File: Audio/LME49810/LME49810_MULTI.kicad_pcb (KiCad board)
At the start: 2 copper layers, 165.1 x 190.5 mm, 124 parts, among them Q1 NPN(TO-3P-BCE), Q2 PNP(TO-3P-BCE), Q3 NPN(TO-220-BCE), U1 LME49810

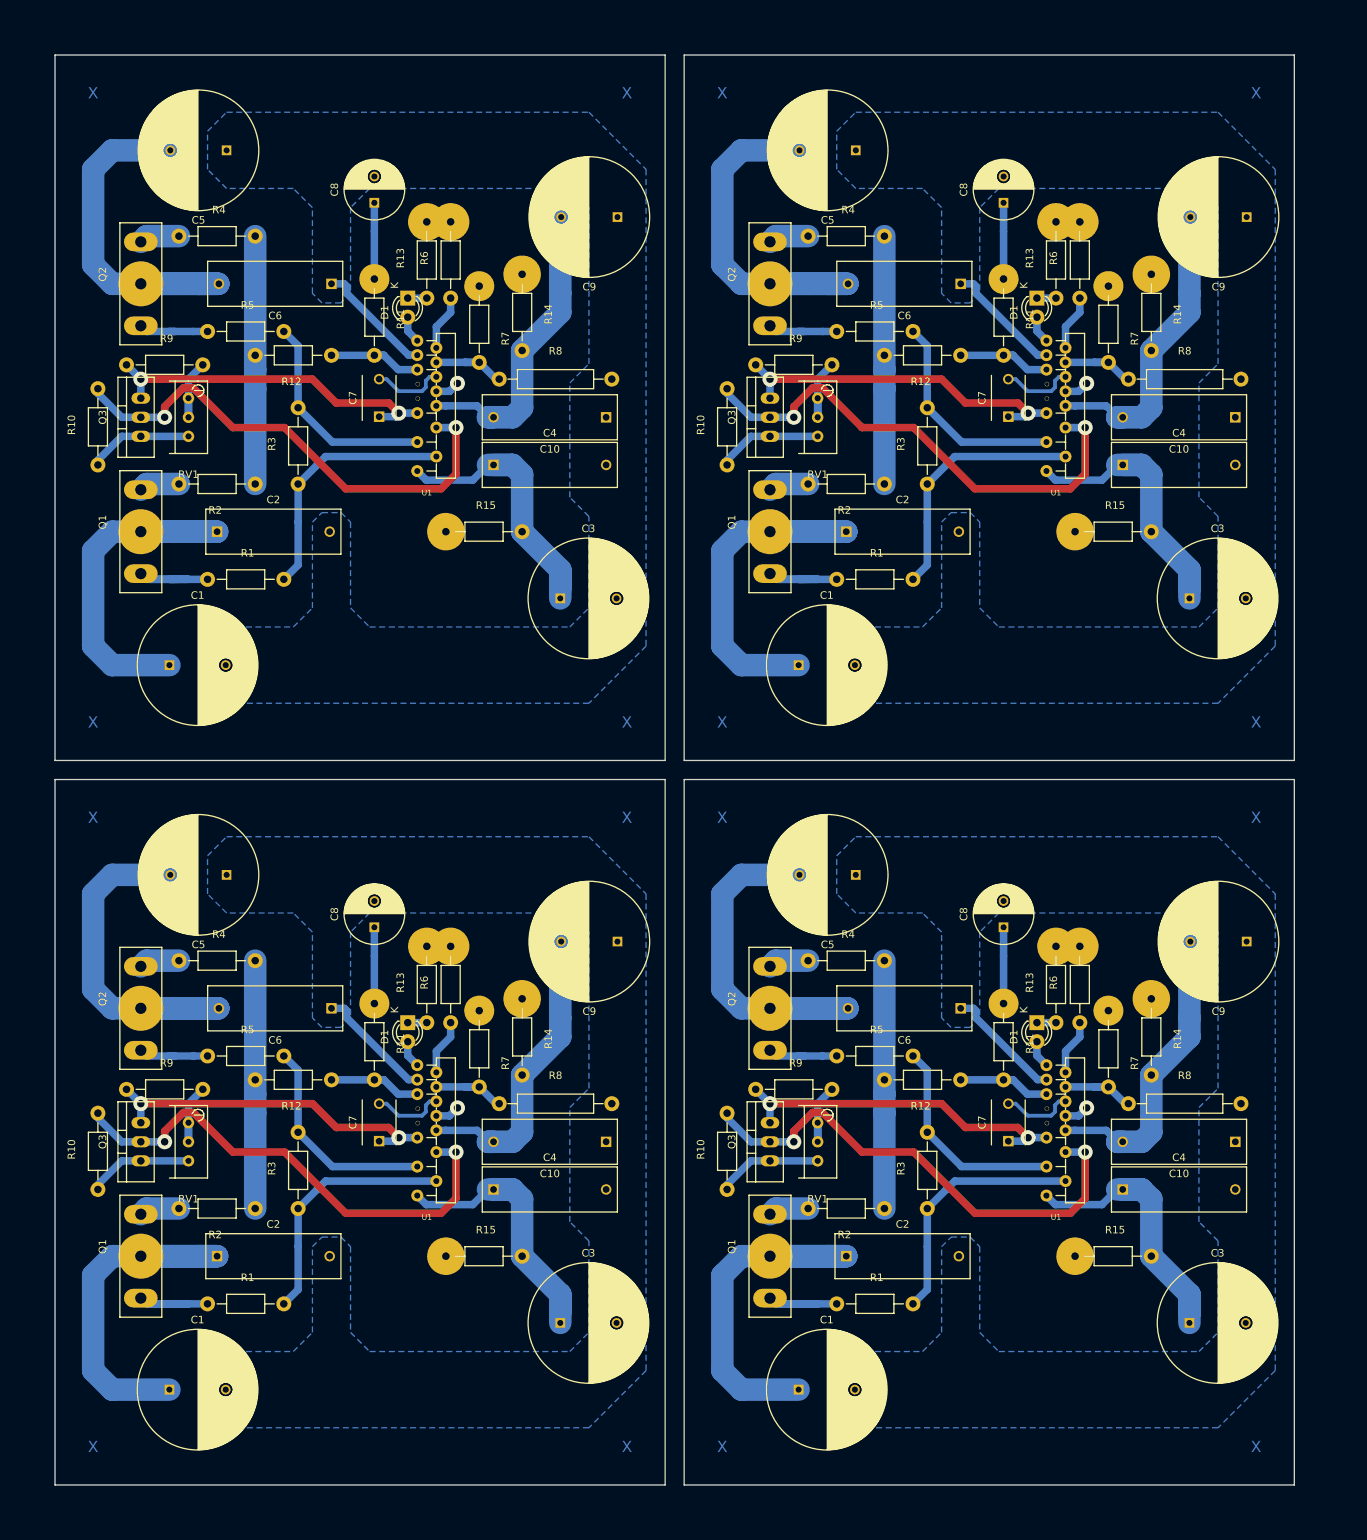
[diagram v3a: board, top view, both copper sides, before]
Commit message: Fixes on component conflict
LME49810 PCB revised
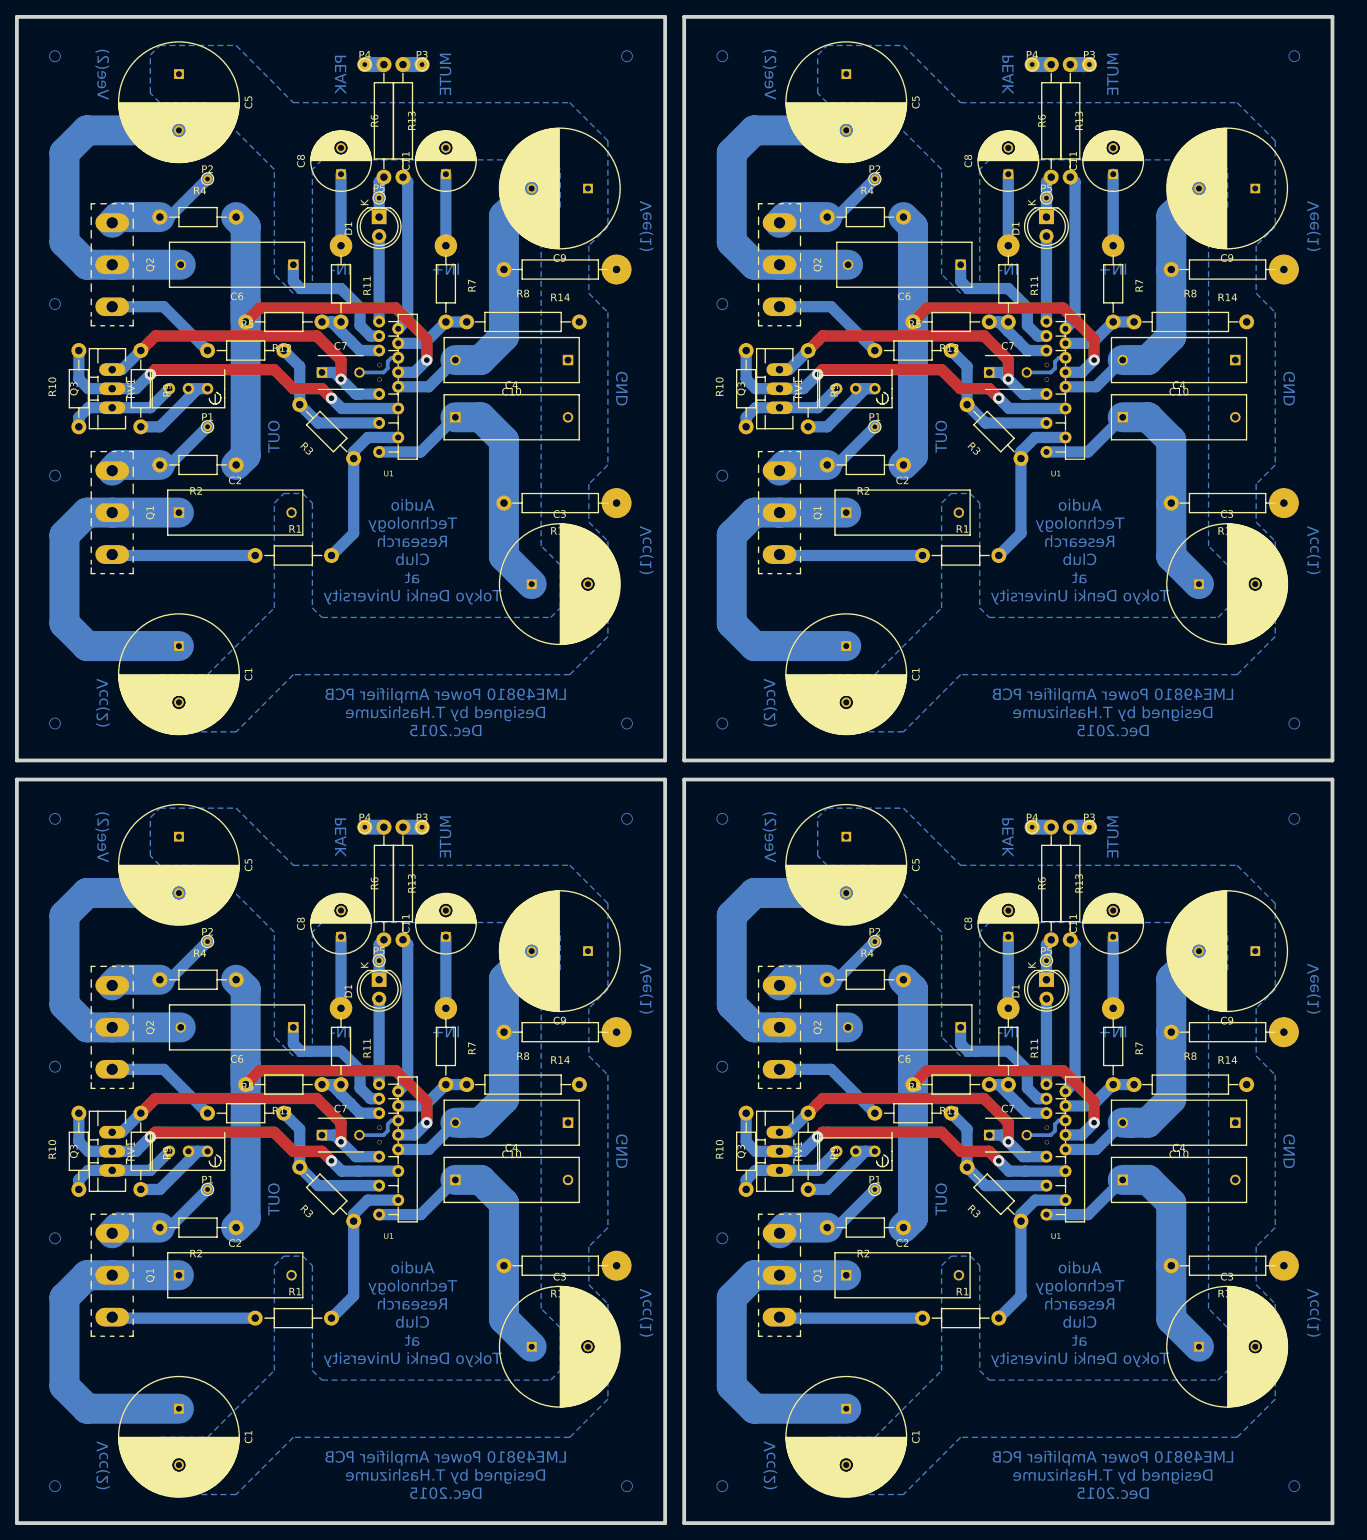
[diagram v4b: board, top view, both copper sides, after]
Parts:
- removed the C1 at (35.6, 101.6)
- removed the C1 at (119.4, 101.6)
- removed the C1 at (35.6, 198.1)
- removed the C1 at (119.4, 198.1)
- removed the C10 at (93.7, 68.6)
- removed the C10 at (177.6, 68.6)
- removed the C10 at (93.7, 165.1)
- removed the C10 at (177.6, 165.1)
- removed the C2 at (41.9, 83.8)
- removed the C2 at (125.7, 83.8)
- removed the C2 at (41.9, 180.3)
- removed the C2 at (125.7, 180.3)
- removed the C3 at (87.6, 92.7)
- removed the C3 at (171.4, 92.7)
- removed the C3 at (87.6, 189.2)
- removed the C3 at (171.4, 189.2)
- removed the C4 at (78.7, 74.9)
- removed the C4 at (162.6, 74.9)
- removed the C4 at (78.7, 171.4)
- removed the C4 at (162.6, 171.4)
- removed the C5 at (43.2, 33.0)
- removed the C5 at (127.0, 33.0)
- removed the C5 at (43.2, 129.5)
- removed the C5 at (127.0, 129.5)
- removed the C6 at (57.1, 50.8)
- removed the C6 at (141.0, 50.8)
- removed the C6 at (57.1, 147.3)
- removed the C6 at (141.0, 147.3)
- removed the C7 at (63.5, 68.5)
- removed the C7 at (147.3, 68.5)
- removed the C7 at (63.5, 165.0)
- removed the C7 at (147.3, 165.0)
- removed the C8 at (62.9, 40.0)
- removed the C8 at (146.7, 40.0)
- removed the C8 at (62.9, 136.5)
- removed the C8 at (146.7, 136.5)
- removed the C9 at (95.2, 41.9)
- removed the C9 at (179.1, 41.9)
- removed the C9 at (95.2, 138.4)
- removed the C9 at (179.1, 138.4)
- removed the D1 at (67.3, 52.7)
- removed the D1 at (151.1, 52.7)
- removed the D1 at (67.3, 149.2)
- removed the D1 at (151.1, 149.2)
- removed the Q1 at (31.8, 83.8)
- removed the Q1 at (115.6, 83.8)
- removed the Q1 at (31.8, 180.3)
- removed the Q1 at (115.6, 180.3)
- removed the Q2 at (31.8, 50.8)
- removed the Q2 at (115.6, 50.8)
- removed the Q2 at (31.8, 147.3)
- removed the Q2 at (115.6, 147.3)
- removed the Q3 at (31.8, 68.6)
- removed the Q3 at (115.6, 68.6)
- removed the Q3 at (31.8, 165.1)
- removed the Q3 at (115.6, 165.1)
- removed the R1 at (45.7, 90.2)
- removed the R1 at (129.5, 90.2)
- removed the R1 at (45.7, 186.7)
- removed the R1 at (129.5, 186.7)
- removed the R10 at (26.0, 69.8)
- removed the R10 at (109.9, 69.8)
- removed the R10 at (26.0, 166.4)
- removed the R10 at (109.9, 166.4)
- removed the R11 at (62.9, 55.2)
- removed the R11 at (146.7, 55.2)
- removed the R11 at (62.9, 151.8)
- removed the R11 at (146.7, 151.8)
- removed the R12 at (52.1, 60.3)
- removed the R12 at (135.9, 60.3)
- removed the R12 at (52.1, 156.8)
- removed the R12 at (135.9, 156.8)
- removed the R13 at (69.8, 47.6)
- removed the R13 at (153.7, 47.6)
- removed the R13 at (69.8, 144.1)
- removed the R13 at (153.7, 144.1)
- removed the R14 at (82.5, 54.6)
- removed the R14 at (166.4, 54.6)
- removed the R14 at (82.5, 151.1)
- removed the R14 at (166.4, 151.1)
- removed the R15 at (77.5, 83.8)
- removed the R15 at (161.3, 83.8)
- removed the R15 at (77.5, 180.3)
- removed the R15 at (161.3, 180.3)
- removed the R2 at (41.9, 77.5)
- removed the R2 at (125.7, 77.5)
- removed the R2 at (41.9, 174.0)
- removed the R2 at (125.7, 174.0)
- removed the R3 at (52.7, 72.4)
- removed the R3 at (136.5, 72.4)
- removed the R3 at (52.7, 168.9)
- removed the R3 at (136.5, 168.9)
- removed the R4 at (41.9, 44.5)
- removed the R4 at (125.7, 44.5)
- removed the R4 at (41.9, 141.0)
- removed the R4 at (125.7, 141.0)
- removed the R5 at (45.7, 57.1)
- removed the R5 at (129.5, 57.1)
- removed the R5 at (45.7, 153.7)
- removed the R5 at (129.5, 153.7)
- removed the R6 at (73.0, 47.6)
- removed the R6 at (156.8, 47.6)
- removed the R6 at (73.0, 144.1)
- removed the R6 at (156.8, 144.1)
- removed the R7 at (76.8, 56.2)
- removed the R7 at (160.7, 56.2)
- removed the R7 at (76.8, 152.7)
- removed the R7 at (160.7, 152.7)
- removed the R8 at (87.0, 63.5)
- removed the R8 at (170.8, 63.5)
- removed the R8 at (87.0, 160.0)
- removed the R8 at (170.8, 160.0)
- removed the R9 at (34.9, 61.6)
- removed the R9 at (118.7, 61.6)
- removed the R9 at (34.9, 158.1)
- removed the R9 at (118.7, 158.1)
- removed the RV1 at (38.1, 66.0)
- removed the RV1 at (121.9, 66.0)
- removed the RV1 at (38.1, 162.6)
- removed the RV1 at (121.9, 162.6)
- removed the U1 at (69.8, 67.1)
- removed the U1 at (153.7, 67.1)
- removed the U1 at (69.8, 163.6)
- removed the U1 at (153.7, 163.6)
- added C1: 820u,100V, Capacitors_ThroughHole:C_Radial_D16_L31.5_P7.5, F.Cu at (36.8, 99.1)
- added C1: 820u,100V, Capacitors_ThroughHole:C_Radial_D16_L31.5_P7.5, F.Cu at (125.7, 99.1)
- added C1: 820u,100V, Capacitors_ThroughHole:C_Radial_D16_L31.5_P7.5, F.Cu at (36.8, 200.7)
- added C1: 820u,100V, Capacitors_ThroughHole:C_Radial_D16_L31.5_P7.5, F.Cu at (125.7, 200.7)
- added C10: 0.1u, Capacitors_ThroughHole:C_Rect_L18_W6_H12_P15, F.Cu at (88.7, 61.0)
- added C10: 0.1u, Capacitors_ThroughHole:C_Rect_L18_W6_H12_P15, F.Cu at (177.6, 61.0)
- added C10: 0.1u, Capacitors_ThroughHole:C_Rect_L18_W6_H12_P15, F.Cu at (88.7, 162.6)
- added C10: 0.1u, Capacitors_ThroughHole:C_Rect_L18_W6_H12_P15, F.Cu at (177.6, 162.6)
- added C11: 470u, Capacitors_ThroughHole:C_Radial_D8_L11.5_P3.5, F.Cu at (72.4, 36.2)
- added C11: 470u, Capacitors_ThroughHole:C_Radial_D8_L11.5_P3.5, F.Cu at (161.3, 36.2)
- added C11: 470u, Capacitors_ThroughHole:C_Radial_D8_L11.5_P3.5, F.Cu at (72.4, 137.8)
- added C11: 470u, Capacitors_ThroughHole:C_Radial_D8_L11.5_P3.5, F.Cu at (161.3, 137.8)
- added C2: 0.1u, Capacitors_ThroughHole:C_Rect_L18_W6_H12_P15, F.Cu at (36.8, 81.3)
- added C2: 0.1u, Capacitors_ThroughHole:C_Rect_L18_W6_H12_P15, F.Cu at (125.7, 81.3)
- added C2: 0.1u, Capacitors_ThroughHole:C_Rect_L18_W6_H12_P15, F.Cu at (36.8, 182.9)
- added C2: 0.1u, Capacitors_ThroughHole:C_Rect_L18_W6_H12_P15, F.Cu at (125.7, 182.9)
- added C3: 820u,100V, Capacitors_ThroughHole:C_Radial_D16_L31.5_P7.5, F.Cu at (83.8, 90.8)
- added C3: 820u,100V, Capacitors_ThroughHole:C_Radial_D16_L31.5_P7.5, F.Cu at (172.7, 90.8)
- added C3: 820u,100V, Capacitors_ThroughHole:C_Radial_D16_L31.5_P7.5, F.Cu at (83.8, 192.4)
- added C3: 820u,100V, Capacitors_ThroughHole:C_Radial_D16_L31.5_P7.5, F.Cu at (172.7, 192.4)
- added C4: 0.1u, Capacitors_ThroughHole:C_Rect_L18_W6_H12_P15, F.Cu at (73.7, 68.6)
- added C4: 0.1u, Capacitors_ThroughHole:C_Rect_L18_W6_H12_P15, F.Cu at (162.6, 68.6)
- added C4: 0.1u, Capacitors_ThroughHole:C_Rect_L18_W6_H12_P15, F.Cu at (73.7, 170.2)
- added C4: 0.1u, Capacitors_ThroughHole:C_Rect_L18_W6_H12_P15, F.Cu at (162.6, 170.2)
- added C5: 820u,100V, Capacitors_ThroughHole:C_Radial_D16_L31.5_P7.5, F.Cu at (36.8, 22.9)
- added C5: 820u,100V, Capacitors_ThroughHole:C_Radial_D16_L31.5_P7.5, F.Cu at (125.7, 22.9)
- added C5: 820u,100V, Capacitors_ThroughHole:C_Radial_D16_L31.5_P7.5, F.Cu at (36.8, 124.5)
- added C5: 820u,100V, Capacitors_ThroughHole:C_Radial_D16_L31.5_P7.5, F.Cu at (125.7, 124.5)
- added C6: 0.1u, Capacitors_ThroughHole:C_Rect_L18_W6_H12_P15, F.Cu at (52.1, 48.3)
- added C6: 0.1u, Capacitors_ThroughHole:C_Rect_L18_W6_H12_P15, F.Cu at (141.0, 48.3)
- added C6: 0.1u, Capacitors_ThroughHole:C_Rect_L18_W6_H12_P15, F.Cu at (52.1, 149.9)
- added C6: 0.1u, Capacitors_ThroughHole:C_Rect_L18_W6_H12_P15, F.Cu at (141.0, 149.9)
- added C7: 10p, Capacitors_ThroughHole:C_Disc_D6_P5, F.Cu at (55.9, 62.6)
- added C7: 10p, Capacitors_ThroughHole:C_Disc_D6_P5, F.Cu at (144.8, 62.6)
- added C7: 10p, Capacitors_ThroughHole:C_Disc_D6_P5, F.Cu at (55.9, 164.2)
- added C7: 10p, Capacitors_ThroughHole:C_Disc_D6_P5, F.Cu at (144.8, 164.2)
- added C8: 220u, Capacitors_ThroughHole:C_Radial_D8_L11.5_P3.5, F.Cu at (58.4, 36.2)
- added C8: 220u, Capacitors_ThroughHole:C_Radial_D8_L11.5_P3.5, F.Cu at (147.3, 36.2)
- added C8: 220u, Capacitors_ThroughHole:C_Radial_D8_L11.5_P3.5, F.Cu at (58.4, 137.8)
- added C8: 220u, Capacitors_ThroughHole:C_Radial_D8_L11.5_P3.5, F.Cu at (147.3, 137.8)
- added C9: 820u,100V, Capacitors_ThroughHole:C_Radial_D16_L31.5_P7.5, F.Cu at (91.3, 38.1)
- added C9: 820u,100V, Capacitors_ThroughHole:C_Radial_D16_L31.5_P7.5, F.Cu at (180.2, 38.1)
- added C9: 820u,100V, Capacitors_ThroughHole:C_Radial_D16_L31.5_P7.5, F.Cu at (91.3, 139.7)
- added C9: 820u,100V, Capacitors_ThroughHole:C_Radial_D16_L31.5_P7.5, F.Cu at (180.2, 139.7)
- added D1: LED, LEDs:LED-5MM, F.Cu at (63.5, 41.9)
- added D1: LED, LEDs:LED-5MM, F.Cu at (152.4, 41.9)
- added D1: LED, LEDs:LED-5MM, F.Cu at (63.5, 143.5)
- added D1: LED, LEDs:LED-5MM, F.Cu at (152.4, 143.5)
- added P1: CONN_01X01, Connect:PINTST, F.Cu at (40.6, 69.8)
- added P1: CONN_01X01, Connect:PINTST, F.Cu at (129.5, 69.8)
- added P1: CONN_01X01, Connect:PINTST, F.Cu at (40.6, 171.4)
- added P1: CONN_01X01, Connect:PINTST, F.Cu at (129.5, 171.4)
- added P2: CONN_01X01, Connect:PINTST, F.Cu at (40.6, 36.8)
- added P2: CONN_01X01, Connect:PINTST, F.Cu at (129.5, 36.8)
- added P2: CONN_01X01, Connect:PINTST, F.Cu at (40.6, 138.4)
- added P2: CONN_01X01, Connect:PINTST, F.Cu at (129.5, 138.4)
- added P3: CONN_01X01, Connect:PINTST, F.Cu at (69.2, 21.6)
- added P3: CONN_01X01, Connect:PINTST, F.Cu at (158.1, 21.6)
- added P3: CONN_01X01, Connect:PINTST, F.Cu at (69.2, 123.2)
- added P3: CONN_01X01, Connect:PINTST, F.Cu at (158.1, 123.2)
- added P4: CONN_01X01, Connect:PINTST, F.Cu at (61.6, 21.6)
- added P4: CONN_01X01, Connect:PINTST, F.Cu at (150.5, 21.6)
- added P4: CONN_01X01, Connect:PINTST, F.Cu at (61.6, 123.2)
- added P4: CONN_01X01, Connect:PINTST, F.Cu at (150.5, 123.2)
- added P5: CONN_01X01, Connect:PINTST, F.Cu at (63.5, 39.4)
- added P5: CONN_01X01, Connect:PINTST, F.Cu at (152.4, 39.4)
- added P5: CONN_01X01, Connect:PINTST, F.Cu at (63.5, 141.0)
- added P5: CONN_01X01, Connect:PINTST, F.Cu at (152.4, 141.0)
- added Q1: NPN(TO-3P-BCE), TO_SOT_Packages_THT:TO-247_Vertical_Neutral123_MountedFromLS, F.Cu at (27.9, 81.3)
- added Q1: NPN(TO-3P-BCE), TO_SOT_Packages_THT:TO-247_Vertical_Neutral123_MountedFromLS, F.Cu at (116.8, 81.3)
- added Q1: NPN(TO-3P-BCE), TO_SOT_Packages_THT:TO-247_Vertical_Neutral123_MountedFromLS, F.Cu at (27.9, 182.9)
- added Q1: NPN(TO-3P-BCE), TO_SOT_Packages_THT:TO-247_Vertical_Neutral123_MountedFromLS, F.Cu at (116.8, 182.9)
- added Q2: PNP(TO-3P-BCE), TO_SOT_Packages_THT:TO-247_Vertical_Neutral123_MountedFromLS, F.Cu at (27.9, 48.3)
- added Q2: PNP(TO-3P-BCE), TO_SOT_Packages_THT:TO-247_Vertical_Neutral123_MountedFromLS, F.Cu at (116.8, 48.3)
- added Q2: PNP(TO-3P-BCE), TO_SOT_Packages_THT:TO-247_Vertical_Neutral123_MountedFromLS, F.Cu at (27.9, 149.9)
- added Q2: PNP(TO-3P-BCE), TO_SOT_Packages_THT:TO-247_Vertical_Neutral123_MountedFromLS, F.Cu at (116.8, 149.9)
- added Q3: NPN(TO-220-BCE), TO_SOT_Packages_THT:TO-220_Neutral123_Vertical_LargePads, F.Cu at (27.9, 64.8)
- added Q3: NPN(TO-220-BCE), TO_SOT_Packages_THT:TO-220_Neutral123_Vertical_LargePads, F.Cu at (116.8, 64.8)
- added Q3: NPN(TO-220-BCE), TO_SOT_Packages_THT:TO-220_Neutral123_Vertical_LargePads, F.Cu at (27.9, 166.4)
- added Q3: NPN(TO-220-BCE), TO_SOT_Packages_THT:TO-220_Neutral123_Vertical_LargePads, F.Cu at (116.8, 166.4)
- added R1: 100, Resistors_ThroughHole:Resistor_Horizontal_RM10mm, F.Cu at (52.1, 87.0)
- added R1: 100, Resistors_ThroughHole:Resistor_Horizontal_RM10mm, F.Cu at (141.0, 87.0)
- added R1: 100, Resistors_ThroughHole:Resistor_Horizontal_RM10mm, F.Cu at (52.1, 188.6)
- added R1: 100, Resistors_ThroughHole:Resistor_Horizontal_RM10mm, F.Cu at (141.0, 188.6)
- added R10: 1.2k, Resistors_ThroughHole:Resistor_Horizontal_RM10mm, F.Cu at (23.5, 64.8)
- added R10: 1.2k, Resistors_ThroughHole:Resistor_Horizontal_RM10mm, F.Cu at (112.4, 64.8)
- added R10: 1.2k, Resistors_ThroughHole:Resistor_Horizontal_RM10mm, F.Cu at (23.5, 166.4)
- added R10: 1.2k, Resistors_ThroughHole:Resistor_Horizontal_RM10mm, F.Cu at (112.4, 166.4)
- added R11: 470, Resistors_ThroughHole:Resistor_Horizontal_RM10mm, F.Cu at (58.4, 50.8)
- added R11: 470, Resistors_ThroughHole:Resistor_Horizontal_RM10mm, F.Cu at (147.3, 50.8)
- added R11: 470, Resistors_ThroughHole:Resistor_Horizontal_RM10mm, F.Cu at (58.4, 152.4)
- added R11: 470, Resistors_ThroughHole:Resistor_Horizontal_RM10mm, F.Cu at (147.3, 152.4)
- added R12: 7.5k, Resistors_ThroughHole:Resistor_Horizontal_RM10mm, F.Cu at (50.8, 55.9)
- added R12: 7.5k, Resistors_ThroughHole:Resistor_Horizontal_RM10mm, F.Cu at (139.7, 55.9)
- added R12: 7.5k, Resistors_ThroughHole:Resistor_Horizontal_RM10mm, F.Cu at (50.8, 157.5)
- added R12: 7.5k, Resistors_ThroughHole:Resistor_Horizontal_RM10mm, F.Cu at (139.7, 157.5)
- added R13: 470, Resistors_ThroughHole:Resistor_Horizontal_RM15mm, F.Cu at (64.1, 29.1)
- added R13: 470, Resistors_ThroughHole:Resistor_Horizontal_RM15mm, F.Cu at (153.0, 29.1)
- added R13: 470, Resistors_ThroughHole:Resistor_Horizontal_RM15mm, F.Cu at (64.1, 130.7)
- added R13: 470, Resistors_ThroughHole:Resistor_Horizontal_RM15mm, F.Cu at (153.0, 130.7)
- added R14: 10, Resistors_ThroughHole:Resistor_Horizontal_RM15mm, F.Cu at (87.6, 48.9)
- added R14: 10, Resistors_ThroughHole:Resistor_Horizontal_RM15mm, F.Cu at (176.5, 48.9)
- added R14: 10, Resistors_ThroughHole:Resistor_Horizontal_RM15mm, F.Cu at (87.6, 150.5)
- added R14: 10, Resistors_ThroughHole:Resistor_Horizontal_RM15mm, F.Cu at (176.5, 150.5)
- added R15: 10, Resistors_ThroughHole:Resistor_Horizontal_RM15mm, F.Cu at (87.6, 80.0)
- added R15: 10, Resistors_ThroughHole:Resistor_Horizontal_RM15mm, F.Cu at (176.5, 80.0)
- added R15: 10, Resistors_ThroughHole:Resistor_Horizontal_RM15mm, F.Cu at (87.6, 181.6)
- added R15: 10, Resistors_ThroughHole:Resistor_Horizontal_RM15mm, F.Cu at (176.5, 181.6)
- added R2: 0.22, Resistors_ThroughHole:Resistor_Horizontal_RM10mm, F.Cu at (39.4, 74.9)
- added R2: 0.22, Resistors_ThroughHole:Resistor_Horizontal_RM10mm, F.Cu at (128.3, 74.9)
- added R2: 0.22, Resistors_ThroughHole:Resistor_Horizontal_RM10mm, F.Cu at (39.4, 176.5)
- added R2: 0.22, Resistors_ThroughHole:Resistor_Horizontal_RM10mm, F.Cu at (128.3, 176.5)
- added R3: 2.2k, Resistors_ThroughHole:Resistor_Horizontal_RM10mm, F.Cu at (56.5, 70.5)
- added R3: 2.2k, Resistors_ThroughHole:Resistor_Horizontal_RM10mm, F.Cu at (145.4, 70.5)
- added R3: 2.2k, Resistors_ThroughHole:Resistor_Horizontal_RM10mm, F.Cu at (56.5, 172.1)
- added R3: 2.2k, Resistors_ThroughHole:Resistor_Horizontal_RM10mm, F.Cu at (145.4, 172.1)
- added R4: 0.22, Resistors_ThroughHole:Resistor_Horizontal_RM10mm, F.Cu at (39.4, 41.9)
- added R4: 0.22, Resistors_ThroughHole:Resistor_Horizontal_RM10mm, F.Cu at (128.3, 41.9)
- added R4: 0.22, Resistors_ThroughHole:Resistor_Horizontal_RM10mm, F.Cu at (39.4, 143.5)
- added R4: 0.22, Resistors_ThroughHole:Resistor_Horizontal_RM10mm, F.Cu at (128.3, 143.5)
- added R5: 100, Resistors_ThroughHole:Resistor_Horizontal_RM10mm, F.Cu at (45.7, 59.7)
- added R5: 100, Resistors_ThroughHole:Resistor_Horizontal_RM10mm, F.Cu at (134.6, 59.7)
- added R5: 100, Resistors_ThroughHole:Resistor_Horizontal_RM10mm, F.Cu at (45.7, 161.3)
- added R5: 100, Resistors_ThroughHole:Resistor_Horizontal_RM10mm, F.Cu at (134.6, 161.3)
- added R6: 33k, Resistors_ThroughHole:Resistor_Horizontal_RM15mm, F.Cu at (66.7, 29.1)
- added R6: 33k, Resistors_ThroughHole:Resistor_Horizontal_RM15mm, F.Cu at (155.6, 29.1)
- added R6: 33k, Resistors_ThroughHole:Resistor_Horizontal_RM15mm, F.Cu at (66.7, 130.7)
- added R6: 33k, Resistors_ThroughHole:Resistor_Horizontal_RM15mm, F.Cu at (155.6, 130.7)
- added R7: 470, Resistors_ThroughHole:Resistor_Horizontal_RM10mm, F.Cu at (72.4, 50.8)
- added R7: 470, Resistors_ThroughHole:Resistor_Horizontal_RM10mm, F.Cu at (161.3, 50.8)
- added R7: 470, Resistors_ThroughHole:Resistor_Horizontal_RM10mm, F.Cu at (72.4, 152.4)
- added R7: 470, Resistors_ThroughHole:Resistor_Horizontal_RM10mm, F.Cu at (161.3, 152.4)
- added R8: 7.5k, Resistors_ThroughHole:Resistor_Horizontal_RM15mm, F.Cu at (82.7, 55.9)
- added R8: 7.5k, Resistors_ThroughHole:Resistor_Horizontal_RM15mm, F.Cu at (171.6, 55.9)
- added R8: 7.5k, Resistors_ThroughHole:Resistor_Horizontal_RM15mm, F.Cu at (82.7, 157.5)
- added R8: 7.5k, Resistors_ThroughHole:Resistor_Horizontal_RM15mm, F.Cu at (171.6, 157.5)
- added R9: 330, Resistors_ThroughHole:Resistor_Horizontal_RM10mm, F.Cu at (31.8, 64.8)
- added R9: 330, Resistors_ThroughHole:Resistor_Horizontal_RM10mm, F.Cu at (120.7, 64.8)
- added R9: 330, Resistors_ThroughHole:Resistor_Horizontal_RM10mm, F.Cu at (31.8, 166.4)
- added R9: 330, Resistors_ThroughHole:Resistor_Horizontal_RM10mm, F.Cu at (120.7, 166.4)
- added RV1: 500, Potentiometers:Potentiometer_Bourns_3296W_3-8Zoll_Inline_ScrewUp, F.Cu at (40.6, 64.8)
- added RV1: 500, Potentiometers:Potentiometer_Bourns_3296W_3-8Zoll_Inline_ScrewUp, F.Cu at (129.5, 64.8)
- added RV1: 500, Potentiometers:Potentiometer_Bourns_3296W_3-8Zoll_Inline_ScrewUp, F.Cu at (40.6, 166.4)
- added RV1: 500, Potentiometers:Potentiometer_Bourns_3296W_3-8Zoll_Inline_ScrewUp, F.Cu at (129.5, 166.4)
- added U1: LME49810, LME49810:LME49810, F.Cu at (64.8, 64.5)
- added U1: LME49810, LME49810:LME49810, F.Cu at (153.7, 64.5)
- added U1: LME49810, LME49810:LME49810, F.Cu at (64.8, 166.1)
- added U1: LME49810, LME49810:LME49810, F.Cu at (153.7, 166.1)
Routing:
- net Net-(C10-Pad2): track 163.5 -> 0.00 mm
- net /Vcc: track 0.00 -> 161.9 mm
- net Net-(C3-Pad1): track 158.2 -> 0.00 mm
- net /Vee: track 0.00 -> 152.5 mm
- net OUTLH: track 165.4 -> 282.0 mm
- net -VeeL2: track 254.7 -> 180.5 mm
- net +VccL2: track 252.3 -> 179.0 mm
- net CLH: track 269.1 -> 200.3 mm
- net /Emit-NPN: track 0.00 -> 60.5 mm
- net /Emit-PNP: track 0.00 -> 60.5 mm
- net Net-(R6-Pad1): track 29.7 -> 84.0 mm
- net SourceLH: track 133.7 -> 87.1 mm
- net Net-(C8-Pad1): track 40.6 -> 0.00 mm
- net /IN-: track 0.00 -> 38.1 mm
- net /IN+: track 0.00 -> 38.1 mm
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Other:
- board size 165.1 x 190.5 mm -> 175.3 x 200.7 mm
- net class Default: trace_width 1 -> 1.5; via_dia 2 -> 1.5; via_drill 1 -> 0.75
- net class Thick: trace_width 3 -> 4
- board text added: "Audio Technology Research Club at Tokyo Denki University"
- board text added: "GND"
- board text added: "IN+"
- board text added: "IN-"
- board text added: "LME49810 Power Amplifier PCB Designed by T.Hashizume Dec.2015"
- board text added: "MUTE"
- board text added: "OUT"
- board text added: "PEAK"
- board text added: "Vcc(1)"
- board text added: "Vcc(2)"
- board text added: "Vee(1)"
- board text added: "Vee(2)"
- board text added: "○"
- board text removed: "X"
